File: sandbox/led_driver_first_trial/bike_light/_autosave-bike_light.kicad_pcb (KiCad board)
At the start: 2 copper layers, 14 parts

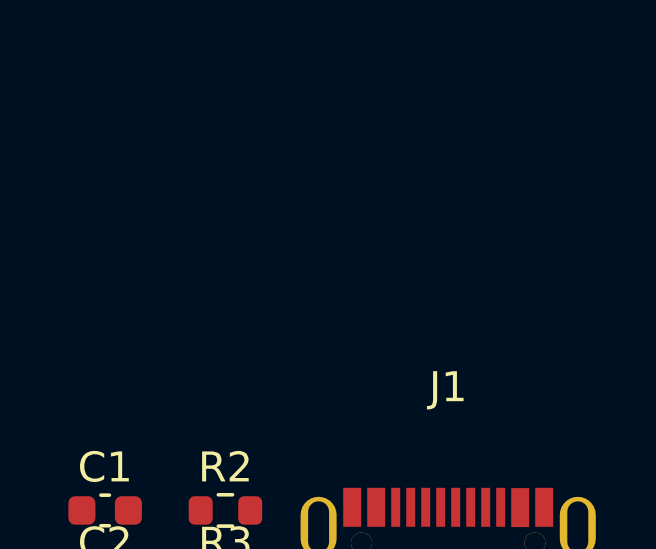
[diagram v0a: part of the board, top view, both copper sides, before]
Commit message: move stubs in schematic around
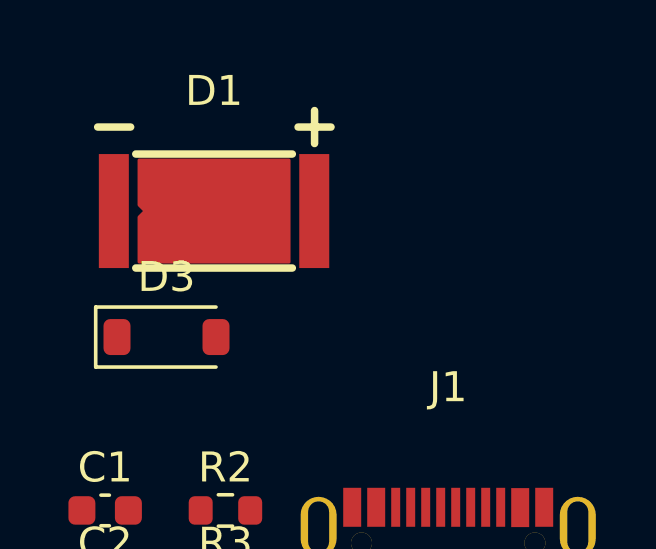
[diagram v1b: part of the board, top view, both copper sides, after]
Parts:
- added D1: , bike_light_lib:LED-SMD_3P-L7.0-W3.5_XL-C3570P5S10-62C3C2, F.Cu at (187.2, 99.1)
- added D3: , Diode_SMD:D_SOD-123, F.Cu at (185.6, 103.3)
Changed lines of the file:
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@@
   (net 16 "37")
   (net 17 "1")
+  (net 18 "4")
   (footprint "bike_light_lib:USB-C-SMD_KH-TYPE-C-16P" (layer "F.Cu")
     (at 194.965 111.355)
@@
       (offset (xyz 0 0 0))
       (scale (xyz 1 1 1))
+      (rotate (xyz 0 0 0))
+    )
+  )
+  (footprint "bike_light_lib:LED-SMD_3P-L7.0-W3.5_XL-C3570P5S10-62C3C2" (layer "F.Cu")
+    (at 187.16 99.06)
+    (attr smd)
+    (fp_text reference "D1" (at 0 -4) (layer "F.SilkS")
+        (effects (font (size 1 1) (thickness 0.15)))
+    )
+    (fp_text value "" (at 0 4) (layer "F.Fab")
+        (effects (font (size 1 1) (thickness 0.15)))
+    )
+    (fp_text user "${REFERENCE}" (at 0 0) (layer "F.Fab")
+        (effects (font (size 1 1) (thickness 0.15)))
+    )
+    (fp_line (start -3.88 -2.8) (end -2.78 -2.8)
+      (stroke (width 0.25) (type solid)) (layer "F.SilkS"))
+    (fp_line (start -2.61 -1.9) (end 2.61 -1.9)
+      (stroke (width 0.25) (type solid)) (layer "F.SilkS"))
+    (fp_line (start -2.61 1.9) (end 2.61 1.9)
+      (stroke (width 0.25) (type solid)) (layer "F.SilkS"))
+    (fp_line (start 2.8 -2.8) (end 3.9 -2.8)
+      (stroke (width 0.25) (type solid)) (layer "F.SilkS"))
+    (fp_line (start 3.35 -2.25) (end 3.35 -3.35)
+      (stroke (width 0.25) (type solid)) (layer "F.SilkS"))
+    (fp_circle (center -3.5 1.75) (end -3.47 1.75)
+      (stroke (width 0.06) (type solid)) (fill none) (layer "F.Fab"))
+    (pad "1" smd rect (at -3.34 0) (size 1 3.8) (layers "F.Cu" "F.Paste" "F.Mask")
+      (net 18 "4"))
+    (pad "2" smd custom (at 0 0) (size 1 1) (layers "F.Cu" "F.Paste" "F.Mask")
+      (net 3 "5") (thermal_bridge_angle 45)
+      (options (clearance outline) (anchor circle))
+      (primitives
+        (gr_poly
+          (pts
+            (xy -2.5 -1.7)
+            (xy 2.5 -1.7)
+            (xy 2.5 1.7)
+            (xy -2.5 1.7)
+            (xy -2.5 0.2)
+            (xy -2.3 0)
+            (xy -2.5 -0.2)
+          )
+          (width 0.1) (fill yes))
+      ))
+    (pad "3" smd rect (at 3.34 0) (size 1 3.8) (layers "F.Cu" "F.Paste" "F.Mask"))
+    (model "libs/bike_light_lib.3dshapes/LED-SMD_3P-L7.0-W3.5_XL-C3570P5S10-62C3C2.wrl"
+      (offset (xyz 0 -0 -0))
+      (scale (xyz 1 1 1))
+      (rotate (xyz 0 0 0))
+    )
+  )
+  (footprint "Diode_SMD:D_SOD-123" (layer "F.Cu")
+    (at 185.575 103.26)
+    (descr "SOD-123")
+    (tags "SOD-123")
+    (attr smd)
+    (fp_text reference "D3" (at 0 -2) (layer "F.SilkS")
+        (effects (font (size 1 1) (thickness 0.15)))
+    )
+    (fp_text value "" (at 0 2.1) (layer "F.Fab")
+        (effects (font (size 1 1) (thickness 0.15)))
+    )
+    (fp_text user "${REFERENCE}" (at 0 -2) (layer "F.Fab")
+        (effects (font (size 1 1) (thickness 0.15)))
+    )
+    (fp_line (start -2.36 -1) (end -2.36 1)
+      (stroke (width 0.12) (type solid)) (layer "F.SilkS"))
+    (fp_line (start -2.36 -1) (end 1.65 -1)
+      (stroke (width 0.12) (type solid)) (layer "F.SilkS"))
+    (fp_line (start -2.36 1) (end 1.65 1)
+      (stroke (width 0.12) (type solid)) (layer "F.SilkS"))
+    (fp_line (start -2.35 -1.15) (end -2.35 1.15)
+      (stroke (width 0.05) (type solid)) (layer "F.CrtYd"))
+    (fp_line (start -2.35 -1.15) (end 2.35 -1.15)
+      (stroke (width 0.05) (type solid)) (layer "F.CrtYd"))
+    (fp_line (start 2.35 -1.15) (end 2.35 1.15)
+      (stroke (width 0.05) (type solid)) (layer "F.CrtYd"))
+    (fp_line (start 2.35 1.15) (end -2.35 1.15)
+      (stroke (width 0.05) (type solid)) (layer "F.CrtYd"))
+    (fp_line (start -1.4 -0.9) (end 1.4 -0.9)
+      (stroke (width 0.1) (type solid)) (layer "F.Fab"))
+    (fp_line (start -1.4 0.9) (end -1.4 -0.9)
+      (stroke (width 0.1) (type solid)) (layer "F.Fab"))
+    (fp_line (start -0.75 0) (end -0.35 0)
+      (stroke (width 0.1) (type solid)) (layer "F.Fab"))
+    (fp_line (start -0.35 0) (end -0.35 -0.55)
+      (stroke (width 0.1) (type solid)) (layer "F.Fab"))
+    (fp_line (start -0.35 0) (end -0.35 0.55)
+      (stroke (width 0.1) (type solid)) (layer "F.Fab"))
+    (fp_line (start -0.35 0) (end 0.25 -0.4)
+      (stroke (width 0.1) (type solid)) (layer "F.Fab"))
+    (fp_line (start 0.25 -0.4) (end 0.25 0.4)
+      (stroke (width 0.1) (type solid)) (layer "F.Fab"))
+    (fp_line (start 0.25 0) (end 0.75 0)
+      (stroke (width 0.1) (type solid)) (layer "F.Fab"))
+    (fp_line (start 0.25 0.4) (end -0.35 0)
+      (stroke (width 0.1) (type solid)) (layer "F.Fab"))
+    (fp_line (start 1.4 -0.9) (end 1.4 0.9)
+      (stroke (width 0.1) (type solid)) (layer "F.Fab"))
+    (fp_line (start 1.4 0.9) (end -1.4 0.9)
+      (stroke (width 0.1) (type solid)) (layer "F.Fab"))
+    (pad "1" smd roundrect (at -1.65 0) (size 0.9 1.2) (layers "F.Cu" "F.Paste" "F.Mask") (roundrect_rratio 0.25)
+      (net 1 "12"))
+    (pad "2" smd roundrect (at 1.65 0) (size 0.9 1.2) (layers "F.Cu" "F.Paste" "F.Mask") (roundrect_rratio 0.25)
+      (net 2 "8"))
+    (model "${KICAD6_3DMODEL_DIR}/Diode_SMD.3dshapes/D_SOD-123.wrl"
+      (offset (xyz 0 0 0))
+      (scale (xyz 1 1 1))

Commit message: start laying out the pcb
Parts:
- added D2: , bike_light_lib:LED-SMD_3P-L7.0-W3.5_XL-C3570P5S10-62C3C2, F.Cu at (120.5, 106.0)
- added D3: , bike_light_lib:LED-SMD_3P-L7.0-W3.5_XL-C3570P5S10-62C3C2, F.Cu at (127.0, 106.0)
- added L1: 2uH, bike_light_lib:IND-SMD_L2.5-W2.0_SLW252012P, F.Cu at (108.0, 110.5)
- added U2: , bike_light_lib:SOT-223_L6.5-W3.5-P2.30-LS7.0-BR, F.Cu at (133.0, 115.0)
- added U3: , bike_light_lib:SOT-23-3_L2.9-W1.3-P1.90-LS2.4-BR, F.Cu at (135.0, 124.5)
- moved J2 89.9 mm to (109.7, 136.0), turned to 90 degrees
- moved D5 82.7 mm to (105.5, 124.0)
- moved U1 80.7 mm to (112.0, 117.5)
- moved R6 75.7 mm to (112.0, 124.0)
- moved D1 73.5 mm to (114.0, 106.0), turned to 90 degrees
- moved J1 73.1 mm to (125.8, 135.1)
- moved D4 71.4 mm to (114.0, 110.5)
- moved R1 71.0 mm to (113.0, 127.5)
- moved R2 65.0 mm to (122.5, 108.0)
- moved C1 60.3 mm to (124.0, 118.5)
- moved C2 56.5 mm to (127.8, 121.0)
- moved C3 56.5 mm to (127.8, 123.5)
- moved C4 56.5 mm to (127.8, 126.0)
- moved R3 56.5 mm to (131.8, 121.0)
- moved R4 56.5 mm to (131.8, 123.5)
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- renumbered D2 to D4, D3 to D5
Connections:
- net 13 renamed 17
- net 27 renamed 31
- net 34 renamed 38
- net 35 renamed 39
- net 36 renamed 40
- net 37 renamed 41
- C2 pad 1: 7 -> 11
- C3 pad 1: 11 -> 15
- D4 pad 1: 15 -> 19
- D4 pad 2: 7 -> 11
- D5 pad 1: 12 -> 16
- D5 pad 2: 8 -> 12
- J2 pad 1: 8 -> 12
- R1 pad 1: 10 -> 14
- R2 pad 1: 7 -> 11
- R3 pad 1: 25 -> 29
- R4 pad 1: 8 -> 12
- R5 pad 1: 7 -> 11
- U1 pad 10: 14 -> 18
- U1 pad 13: 7 -> 11
- U1 pad 18: 15 -> 19
- U1 pad 4: 10 -> 14
- U1 pad 6: 11 -> 15
- U1 pad 7: 12 -> 16
- U1 pad 9: 14 -> 18
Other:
- board outline added: 40 x 40 mm
